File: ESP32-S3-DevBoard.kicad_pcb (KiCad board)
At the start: 2 copper layers, 32 x 57.1 mm, 27 parts, among them J1 USB_C_Receptacle_USB2.0_14P, J2 Conn_01x22_Socket, J3 Conn_01x22_Socket, U1 ESP32-S3-WROOM-1, U2 AMS1117-3.3

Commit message: Convert to 4 layer design
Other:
- copper layers 2 -> 4
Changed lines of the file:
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@@
 	(layers
 		(0 "F.Cu" signal)
+		(1 "In1.Cu" power "GND")
+		(2 "In2.Cu" power "PWR")
 		(31 "B.Cu" signal)
 		(32 "B.Adhes" user "B.Adhesive")
@@
 	)
 	(setup
+		(stackup
+			(layer "F.SilkS"
+				(type "Top Silk Screen")
+			)
+			(layer "F.Paste"
+				(type "Top Solder Paste")
+			)
+			(layer "F.Mask"
+				(type "Top Solder Mask")
+				(thickness 0.01)
+			)
+			(layer "F.Cu"
+				(type "copper")
+				(thickness 0.035)
+			)
+			(layer "dielectric 1"
+				(type "prepreg")
+				(thickness 0.1)
+				(material "FR4")
+				(epsilon_r 4.5)
+				(loss_tangent 0.02)
+			)
+			(layer "In1.Cu"
+				(type "copper")
+				(thickness 0.035)
+			)
+			(layer "dielectric 2"
+				(type "core")
+				(thickness 1.24)
+				(material "FR4")
+				(epsilon_r 4.5)
+				(loss_tangent 0.02)
+			)
+			(layer "In2.Cu"
+				(type "copper")
+				(thickness 0.035)
+			)
+			(layer "dielectric 3"
+				(type "prepreg")
+				(thickness 0.1)
+				(material "FR4")
+				(epsilon_r 4.5)
+				(loss_tangent 0.02)
+			)
+			(layer "B.Cu"
+				(type "copper")
+				(thickness 0.035)
+			)
+			(layer "B.Mask"
+				(type "Bottom Solder Mask")
+				(thickness 0.01)
+			)
+			(layer "B.Paste"
+				(type "Bottom Solder Paste")
+			)
+			(layer "B.SilkS"
+				(type "Bottom Silk Screen")
+			)
+			(copper_finish "None")
+			(dielectric_constraints no)
+		)
 		(pad_to_mask_clearance 0)
 		(allow_soldermask_bridges_in_footprints no)
@@
 		)
 		(fp_text user "10k"
-			(at 0 0 270)
+			(at 0 0 -90)
 			(unlocked yes)
 			(layer "F.SilkS")

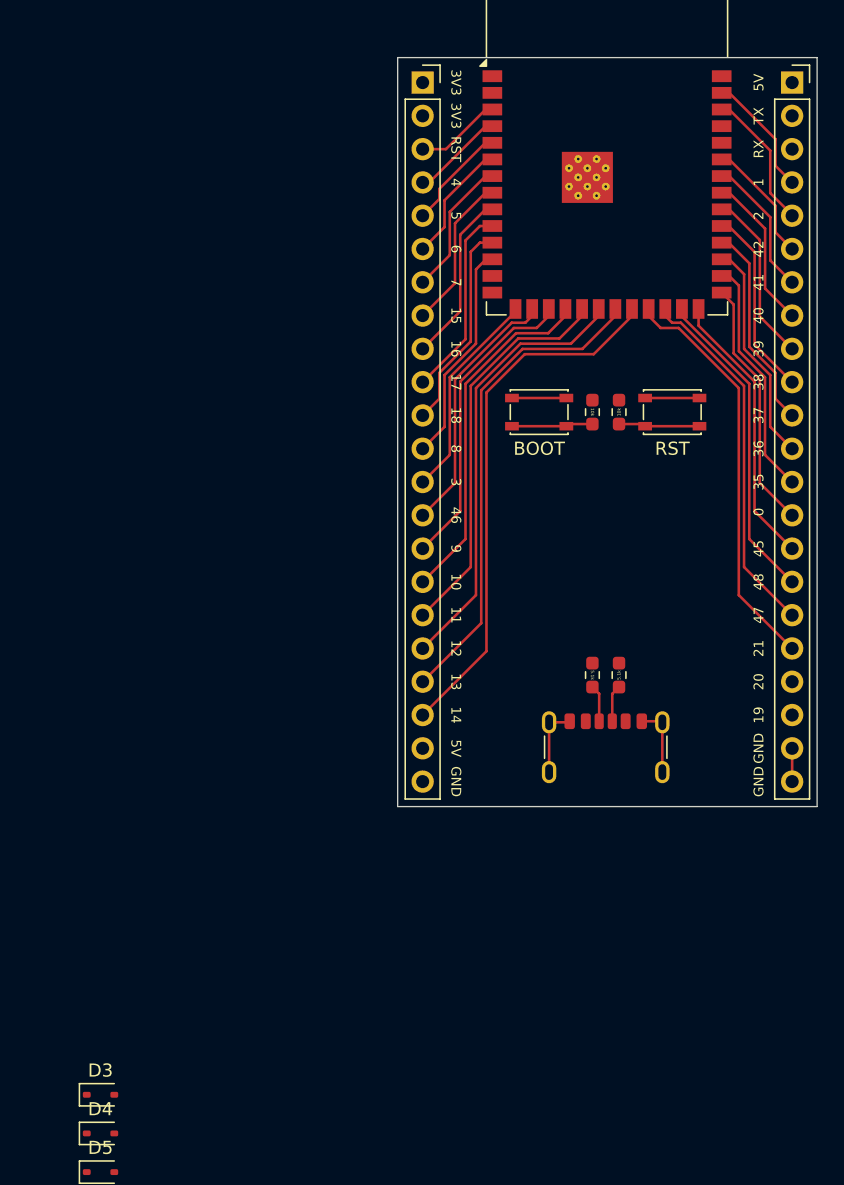
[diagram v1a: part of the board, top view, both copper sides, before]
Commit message: Update USB-C footprint
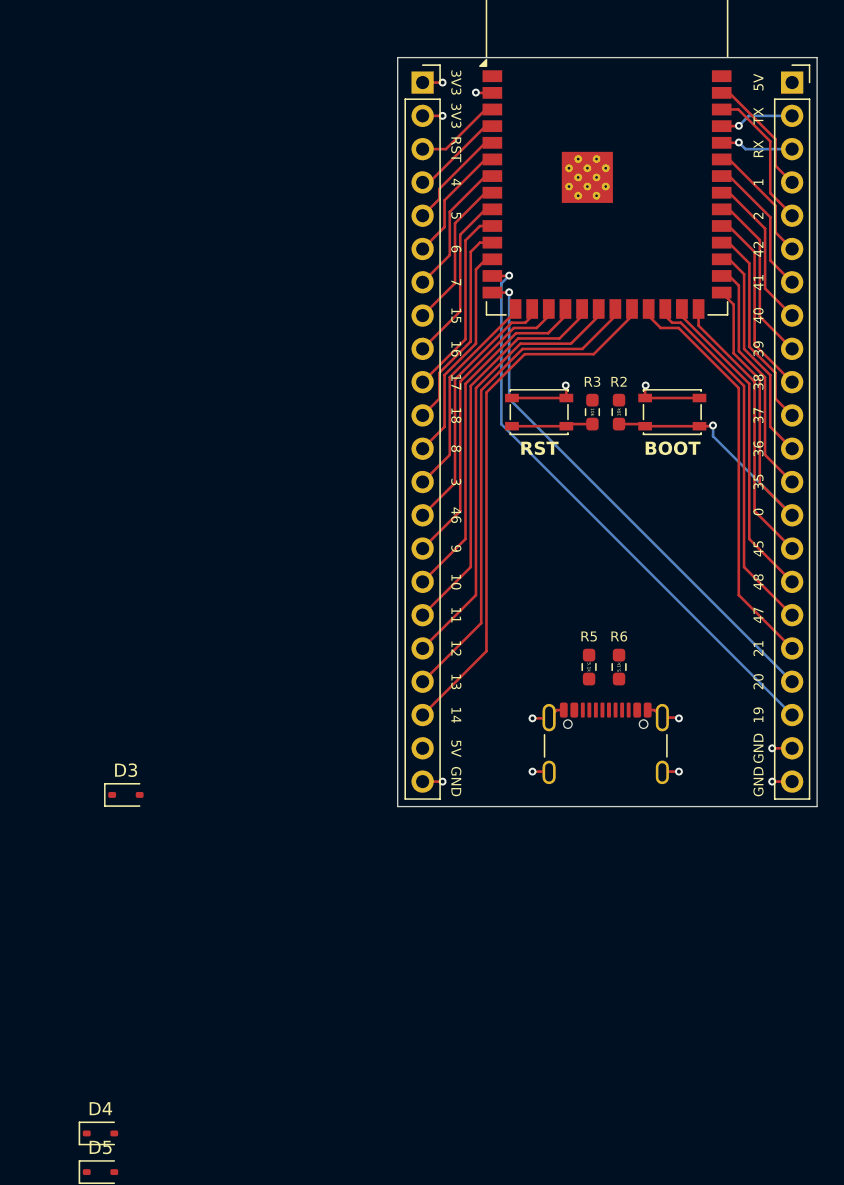
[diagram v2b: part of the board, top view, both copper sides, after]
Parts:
- J1: footprint Connector_USB:USB_C_Receptacle_GCT_USB4125-xx-x_6P_TopMnt_Horizontal -> Connector_USB:USB_C_Receptacle_GCT_USB4105-xx-A_16P_TopMnt_Horizontal
- moved D3 23.0 mm to (153.9, 109.2)
- moved R5 0.66 mm to (189.2, 99.5)
- moved R6 0.61 mm to (191.5, 99.5)
- moved J1 0.25 mm to (190.5, 106.4)
- renumbered RST to BOOT, BOOT to RST
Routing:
- net GPIO_19: track 0.00 -> 44.3 mm, vias 0 -> 1
- net GPIO_20: track 0.00 -> 40.0 mm, vias 0 -> 1
- net GPIO_0: track 25.4 -> 36.0 mm, vias 0 -> 1
- net UART0_TX: track 0.00 -> 5.70 mm, vias 0 -> 1
- net UART0_RX: track 0.00 -> 5.59 mm, vias 0 -> 1
- net ESP_3.3V: track 0.00 -> 4.31 mm, vias 0 -> 3
- net Net-(J1-CC2): track 2.83 -> 0.00 mm
- net Net-(J1-CC1): track 2.83 -> 0.00 mm
- net GND: track 23.1 -> 24.2 mm, vias 0 -> 9
- added copper zone on In1.Cu, net GND
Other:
- board text added: "BOOT"

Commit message: Finish layout
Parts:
- D3, D4, D5: footprint Diode_SMD:D_SOD-323 -> Diode_SMD:D_SOD-323_HandSoldering
- moved C5 116.5 mm to (198.4, 102.4), turned to 180 degrees
- moved C3 115.0 mm to (191.8, 79.8), turned to -90 degrees
- moved C4 113.6 mm to (189.2, 79.8), turned to -90 degrees
- moved C9 112.6 mm to (197.6, 95.1), turned to -90 degrees
- moved C6 110.4 mm to (198.4, 104.4), turned to 180 degrees
- moved R4 109.2 mm to (196.6, 86.4)
- moved R1 103.5 mm to (184.4, 86.4), turned to 180 degrees
- moved C8 100.5 mm to (184.4, 90.4), turned to 180 degrees
- moved C7 100.3 mm to (184.4, 88.4), turned to 180 degrees
- moved C2 99.3 mm to (182.6, 104.4)
- moved C1 99.3 mm to (182.6, 102.4)
- moved D1 89.1 mm to (196.6, 88.4)
- moved D2 80.4 mm to (193.5, 94.6)
- moved U2 77.4 mm to (190.5, 87.4), turned to 90 degrees
- moved D5 56.2 mm to (187.5, 94.5), turned to 180 degrees
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- renumbered BOOT to SW1, RST to SW2
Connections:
- J3 pad 1: VCC_5V -> GND
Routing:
- net VCC_5V: track 0.00 -> 42.1 mm, vias 0 -> 1
- net VCC_3.3V: track 0.00 -> 37.9 mm
- net CHIP_PU: track 12.8 -> 42.1 mm, vias 0 -> 1
- net GND: track 24.2 -> 51.4 mm, vias 9 -> 23
- net VBUS: track 0.00 -> 26.1 mm
- net GPIO_20: track 40.0 -> 64.8 mm, vias 1 -> 2
- net GPIO_19: track 44.3 -> 66.6 mm, vias 1 -> 2
- net Net-(J1-CC1): track 0.00 -> 4.17 mm
- net Net-(J1-CC2): track 0.00 -> 3.88 mm
- net ESP_3.3V: track 4.31 -> 7.77 mm, vias 3 -> 6
- net GPIO_0: track 36.0 -> 38.8 mm
- net Net-(D1-A): track 0.00 -> 2.05 mm
- added copper zone on In2.Cu, net ESP_3.3V
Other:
- board text added: "PWR"
